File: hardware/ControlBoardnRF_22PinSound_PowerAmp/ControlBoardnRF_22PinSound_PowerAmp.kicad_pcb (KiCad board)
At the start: 2 copper layers, 72.6 x 89.1 mm, 44 parts, among them J1 RC, J10 BT Switch, J11 Motor3, J13 Main Power, J14 Volume, J15 Left Speaker, J2 LinAct, J3 Speed Ctrl, J4 Aux A5, J5 I2C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

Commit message: Component placement changes and updates
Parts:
- removed ? (x2): , MountingHole:MountingHole_3mm
- removed JP5: 5v Jumper, Jumper:SolderJumper-2_P1.3mm_Open_TrianglePad1.0x1.5mm
- removed U3: TMR_1-0511_mod, Useful Modifications:Regulator_LM2596Adj
- added JP1: Throttle Jumper, Connector_PinHeader_2.54mm:PinHeader_1x03_P2.54mm_Vertical, F.Cu at (166.1, 95.9)
- added JP2: Steering Jumper, Connector_PinHeader_2.54mm:PinHeader_1x03_P2.54mm_Vertical, F.Cu at (166.1, 101.0)
- added JP3: LTC Throttle Jumper, Connector_PinHeader_2.54mm:PinHeader_1x02_P2.54mm_Vertical, F.Cu at (176.3, 95.9)
- added JP4: LTC Steering Jumper, Connector_PinHeader_2.54mm:PinHeader_1x02_P2.54mm_Vertical, F.Cu at (176.3, 101.0)
- added REF**: MountingHole_2.5mm, MountingHole:MountingHole_2.5mm, F.Cu at (122.7, 154.2)
- added REF**: MountingHole_2.5mm, MountingHole:MountingHole_2.5mm, F.Cu at (177.0, 72.7)
- added REF**: MountingHole_2.5mm, MountingHole:MountingHole_2.5mm, F.Cu at (112.2, 72.7)
- added REF**: MountingHole_2.5mm, MountingHole:MountingHole_2.5mm, F.Cu at (177.0, 154.2)
- added TP3: 5v, TestPoint:TestPoint_Pad_1.5x1.5mm, F.Cu at (141.3, 149.8)
- added U2: LTC2645CMS-L8-PBF, Useful Modifications:LTC2645CMS-L8-PBF, B.Cu at (150.8, 93.6)
- J11: value Motor3 -> LinAct_M3
- J3: value Speed Ctrl -> SpeedCtrl
- J4: value Aux A5 -> Power Input; footprint Connector_PinHeader_2.54mm:PinHeader_1x03_P2.54mm_Vertical -> Connector_PinHeader_2.54mm:PinHeader_1x04_P2.54mm_Horizontal
- J6: value Motor1 -> Left_M1
- J8: value Motor2 -> Right_M2
- moved J4 35.7 mm to (136.0, 135.4), turned to 270 degrees
- moved TP1 30.1 mm to (146.1, 149.8), turned to 90 degrees
- moved J1 15.2 mm to (166.1, 111.1)
- moved J14 15.2 mm to (166.1, 126.4)
- moved J2 15.2 mm to (166.1, 116.2)
- moved J3 15.2 mm to (166.1, 121.3)
- moved J10 12.8 mm to (142.8, 82.1)
- moved J5 12.7 mm to (166.1, 134.0)
- moved U1 11.7 mm to (151.2, 121.0)
- moved TP2 7.71 mm to (142.8, 87.5)
- moved J7 6.83 mm to (166.6, 80.3), turned to 200 degrees
- moved J15 5.22 mm to (126.2, 78.0), turned to 45 degrees
- moved J11 5.00 mm to (113.2, 123.8)
- moved C1 5.00 mm to (128.9, 112.2)
- moved C10 5.00 mm to (124.9, 88.7)
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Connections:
- net M1_DIR renamed Left_DIR
- net M1_PWM renamed Left_PWM
- net M2_DIR renamed Right_DIR
- net M2_PWM renamed Right_PWM
- net M3_DIR renamed LinAct_DIR
- net M3_PWM renamed LinAct_PWM
- J1 pad 3: RC_Throttle -> RCPWMThrottle
- J1 pad 4: RC_Steering -> RCPWMSteering
- J4 pad 1: +3V3 -> GND
- J4 pad 2: AuxA5 -> +5V
- J4 pad 3: GND -> +12V
- J7 pad 5: Throttle -> Net-(J7-Pad5)
- J7 pad 6: Steering -> Net-(J7-Pad6)
- J7 pad 8: AuxA5 -> ActiveSW
- U1 pad 10: AuxA5 -> RCAnalogSteering
- U1 pad 14: Net-(U1-Pad14) -> ActiveSW
- U1 pad 16: RC_Throttle -> Net-(U1-Pad16)
- U1 pad 19: RC_Steering -> BT_Switch
- U1 pad 9: BT_Switch -> RCAnalogThrottle
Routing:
- net ActiveSW: track 0.00 -> 84.9 mm, vias 0 -> 2
- net AuxA5: track 68.1 -> 0.00 mm
- net RC_Throttle: track 56.9 -> 0.00 mm
- net RCAnalogSteering: track 0.00 -> 44.4 mm, vias 0 -> 1
- net RCAnalogThrottle: track 0.00 -> 41.8 mm, vias 0 -> 1
- net PWMThrottle: track 0.00 -> 40.4 mm
- net RC_Steering: track 37.1 -> 0.00 mm
- net Net-(JP4-Pad1): track 0.00 -> 34.2 mm, vias 0 -> 1
- net Net-(JP3-Pad1): track 0.00 -> 33.3 mm, vias 0 -> 1
- net PWMSteering: track 0.00 -> 29.3 mm, vias 0 -> 1
- net RCPWMSteering: track 0.00 -> 27.9 mm, vias 0 -> 2
- net Net-(J7-Pad5): track 0.00 -> 25.6 mm
- net RCPWMThrottle: track 0.00 -> 25.3 mm, vias 0 -> 2
- net +5V: track 149.5 -> 124.7 mm, vias 2 -> 3
- net Sound2: track 86.9 -> 72.0 mm, vias 2 -> 0
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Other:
- board text added: "3 G S"
- board text added: "A C PWM"
- board text added: "PWM"
- board text added: "Steering"
- board text added: "Throttle"
- board text added: "nRF28PwPAmp 2"
- board text removed: "5v"
- board text removed: "nRF28PwPAmp 1"

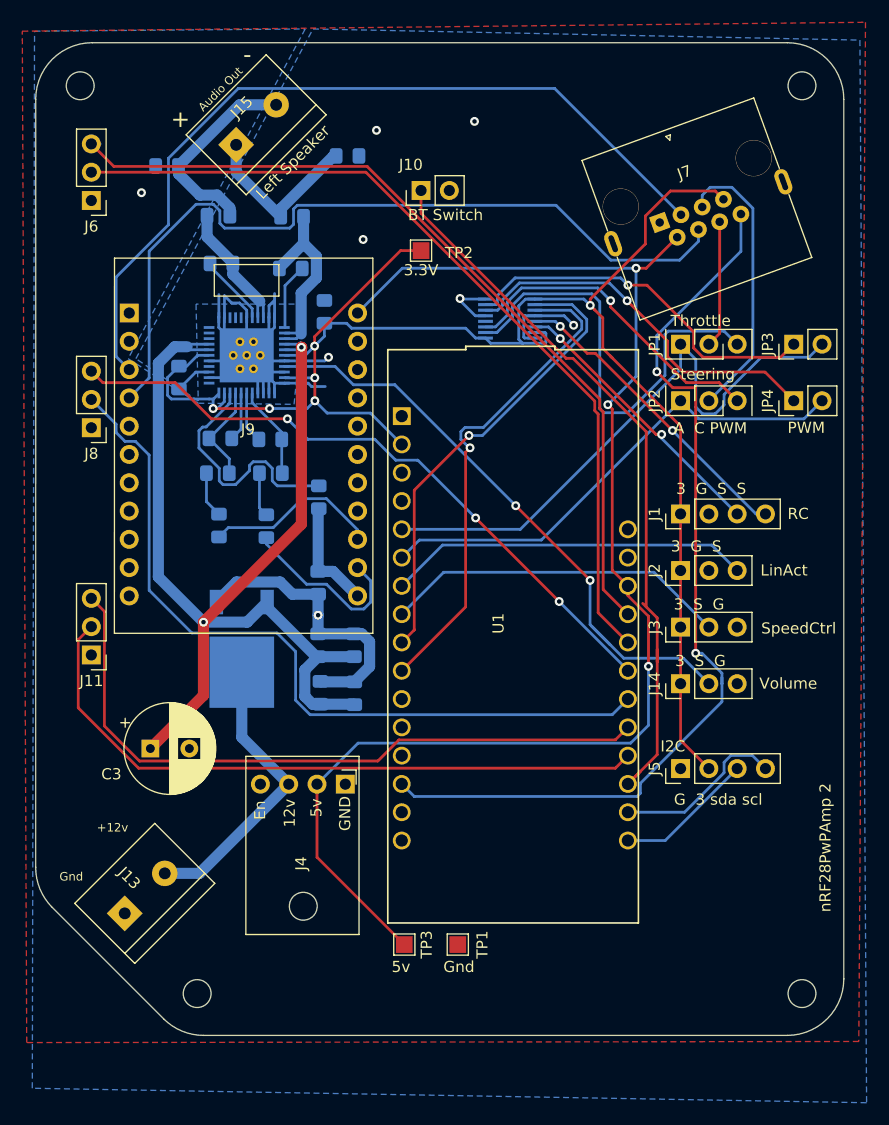
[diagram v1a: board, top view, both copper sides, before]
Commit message: Minor pin adjustments
Shifted all input pins way from RJ45 connector. Shifted BT Switch closer to RJ45 connector. Made the holds for the Feather 1mm instead of 1.1mm. Adjusted the screw hole on the MPM3610. Added the text USB on the usb side of the feather.
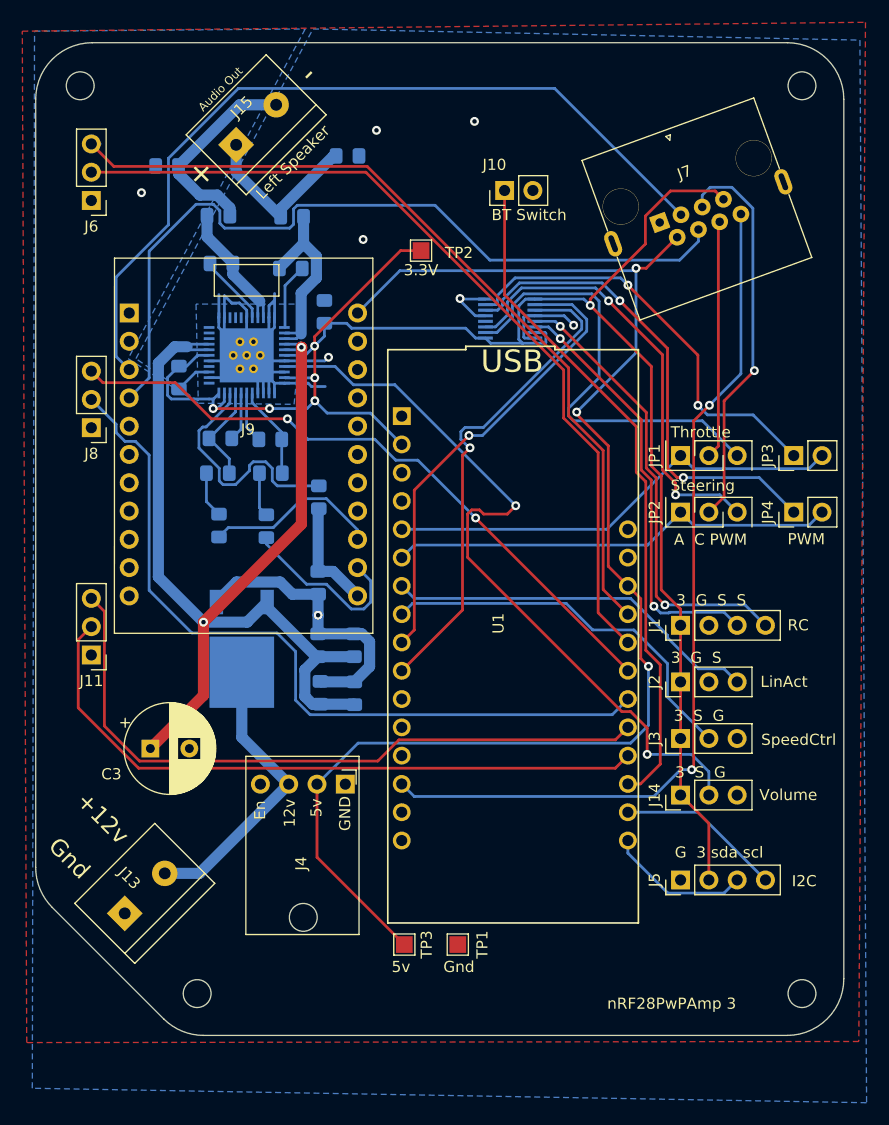
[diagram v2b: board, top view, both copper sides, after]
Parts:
- J4: footprint Connector_PinHeader_2.54mm:PinHeader_1x04_P2.54mm_Horizontal -> Useful Modifications:AdaFruit_MPM3610
- moved J3 10.0 mm to (166.1, 131.3)
- moved J1 10.0 mm to (166.1, 121.1)
- moved J14 10.0 mm to (166.1, 136.4)
- moved J2 10.0 mm to (166.1, 126.2)
- moved J5 10.0 mm to (166.1, 144.0)
- moved JP1 10.0 mm to (166.1, 105.9)
- moved JP2 10.0 mm to (166.1, 111.0)
- moved JP3 10.0 mm to (176.3, 105.9)
- moved JP4 10.0 mm to (176.3, 111.0)
- moved J10 7.50 mm to (150.3, 82.1)
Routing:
- net Net-(J14-Pad2): track 54.6 -> 67.9 mm
- net RCPWMSteering: track 27.9 -> 41.2 mm
- net RCPWMThrottle: track 25.3 -> 38.5 mm
- net Throttle: track 54.2 -> 41.9 mm
- net PWMSteering: track 29.3 -> 39.7 mm, vias 1 -> 2
- net Net-(J7-Pad5): track 25.6 -> 35.7 mm, vias 0 -> 1
- net Net-(J7-Pad6): track 11.4 -> 21.4 mm
- net +3V3: track 157.5 -> 167.2 mm
- net Net-(JP4-Pad1): track 34.2 -> 43.8 mm, vias 1 -> 2
- net BT_Switch: track 66.6 -> 60.9 mm
- net ActiveSW: track 84.9 -> 79.2 mm
- net Net-(JP3-Pad1): track 33.3 -> 38.3 mm, vias 1 -> 2
- net Steering: track 44.9 -> 40.4 mm
- net SpeedCtrl: track 31.2 -> 34.8 mm
- net +5V: track 124.7 -> 127.0 mm
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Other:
- board text added: "USB"
- board text added: "nRF28PwPAmp 3"
- board text removed: "nRF28PwPAmp 2"

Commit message: isolating 12v and amp from microcontroller
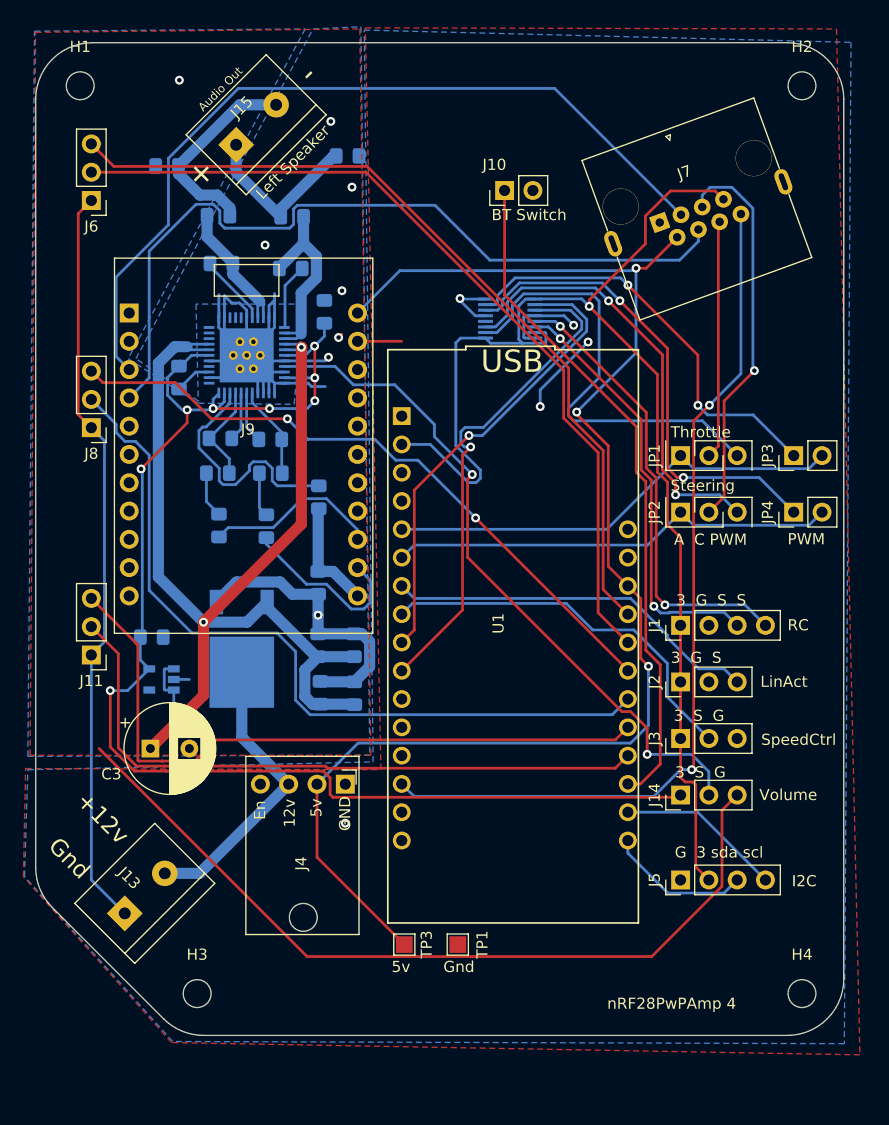
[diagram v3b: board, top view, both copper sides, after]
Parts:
- removed REF** (x4): MountingHole_2.5mm, MountingHole:MountingHole_2.5mm
- removed TP2: 3.3V, TestPoint:TestPoint_Pad_1.5x1.5mm
- added C11: 10µF, Capacitor_SMD:C_0805_2012Metric_Pad1.15x1.40mm_HandSolder, B.Cu at (118.6, 122.2)
- added H1: MountingHole, MountingHole:MountingHole_2.5mm, F.Cu at (112.2, 72.7)
- added H2: MountingHole, MountingHole:MountingHole_2.5mm, F.Cu at (177.0, 72.7)
- added H3: MountingHole, MountingHole:MountingHole_2.5mm, F.Cu at (122.7, 154.2)
- added H4: MountingHole, MountingHole:MountingHole_2.5mm, F.Cu at (177.0, 154.2)
- added U3: AP2112K-3.3, Package_TO_SOT_SMD:SOT-23-5, B.Cu at (119.5, 126.0)
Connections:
- J14 pad 1: +3V3 -> +3.3VP
- R10 pad 2: +3V3 -> +3.3VP
- R9 pad 1: +3V3 -> +3.3VP
- U4 pad 10: +3V3 -> +3.3VP
- U4 pad 21: +3V3 -> +3.3VP
- U4 pad 22: +3V3 -> +3.3VP
- U4 pad 28: +3V3 -> +3.3VP
- U4 pad 6: +3V3 -> +3.3VP
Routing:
- net GND: track 110.3 -> 265.9 mm, vias 8 -> 13
- net +3.3VP: track 0.00 -> 126.3 mm, vias 0 -> 8
- net +3V3: track 167.2 -> 116.6 mm, vias 6 -> 1
- net Net-(C3-Pad1): track 102.4 -> 112.0 mm
- net Net-(J14-Pad2): track 67.9 -> 62.3 mm
- net LinAct_DIR: track 59.8 -> 58.9 mm
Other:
- board text added: "nRF28PwPAmp 4"
- board text removed: "nRF28PwPAmp 3"
